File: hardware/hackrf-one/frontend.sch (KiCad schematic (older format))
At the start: 144 parts, among them J10 GND_CLIP, J2 RF-SHIELD-FRAME, J3 RF-SHIELD-COVER, J4 MOUNTING_HOLE, J5 MOUNTING_HOLE, J6 MOUNTING_HOLE, J7 MOUNTING_HOLE, J8 MOUNTING_HOLE, J9 MOUNTING_HOLE, P13 GPO1, P17 GPO6, P19 GPO3, P21 REF_IN, P27 MIXER_SDATA, P31 MIXER_SCLK, P32 MIXER_ENX, P33 MIXER_RESETX, P34 MIX_BYPASS, P35 !MIX_BYPASS, P4 ANTENNA, P42 TX, P43 RX, P44 HP, P45 LP, P46 TX_MIX_BP, P47 RX_MIX_BP, P48 TX_AMP, P49 RX_AMP, P50 AMP_BYPASS, P51 !TX_AMP_PWR, P52 !RX_AMP_PWR, P6 GPO4, P7 GPO2, Q1 MOSFET_P, Q2 MOSFET_P, Q4 MOSFET_P, T1 MIX_IN_BALUN, T2 MIX_OUT_BALUN, U1 SKY13350, U10 SKY13350, U11 SKY13350, U12 SKY13317, U13 MGA-81563, U14 SKY13317, U2 SKY13350, U25 MGA-81563, U3 RX_LOWPASS_FILTER, U4 RFFC5072, U5 SKY13350, U6 SKY13350, U7 SKY13350, U8 RX_HIGHPASS_FILTER, U9 SKY13317

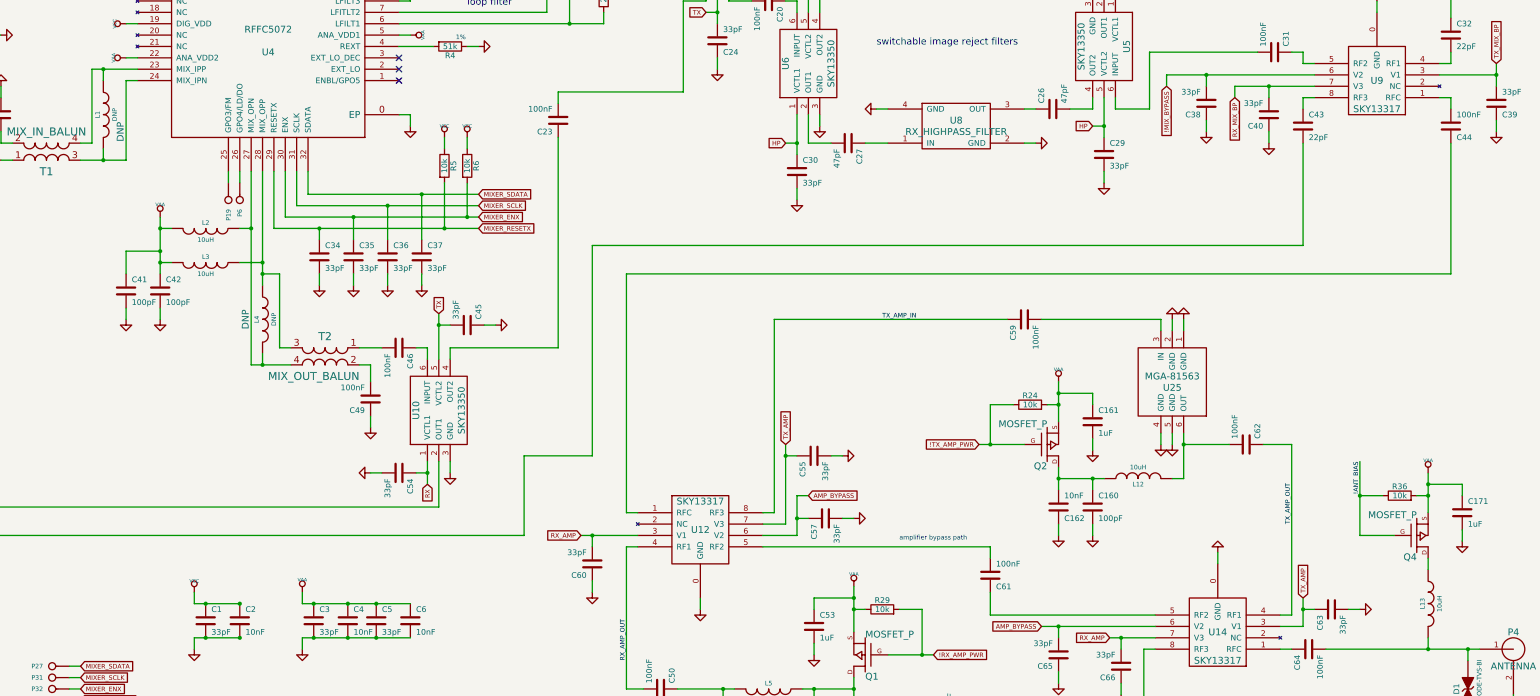
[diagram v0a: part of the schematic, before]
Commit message: HackRF One: changed U25 TX RF amplifier from MGA-81563 to TRF37A73
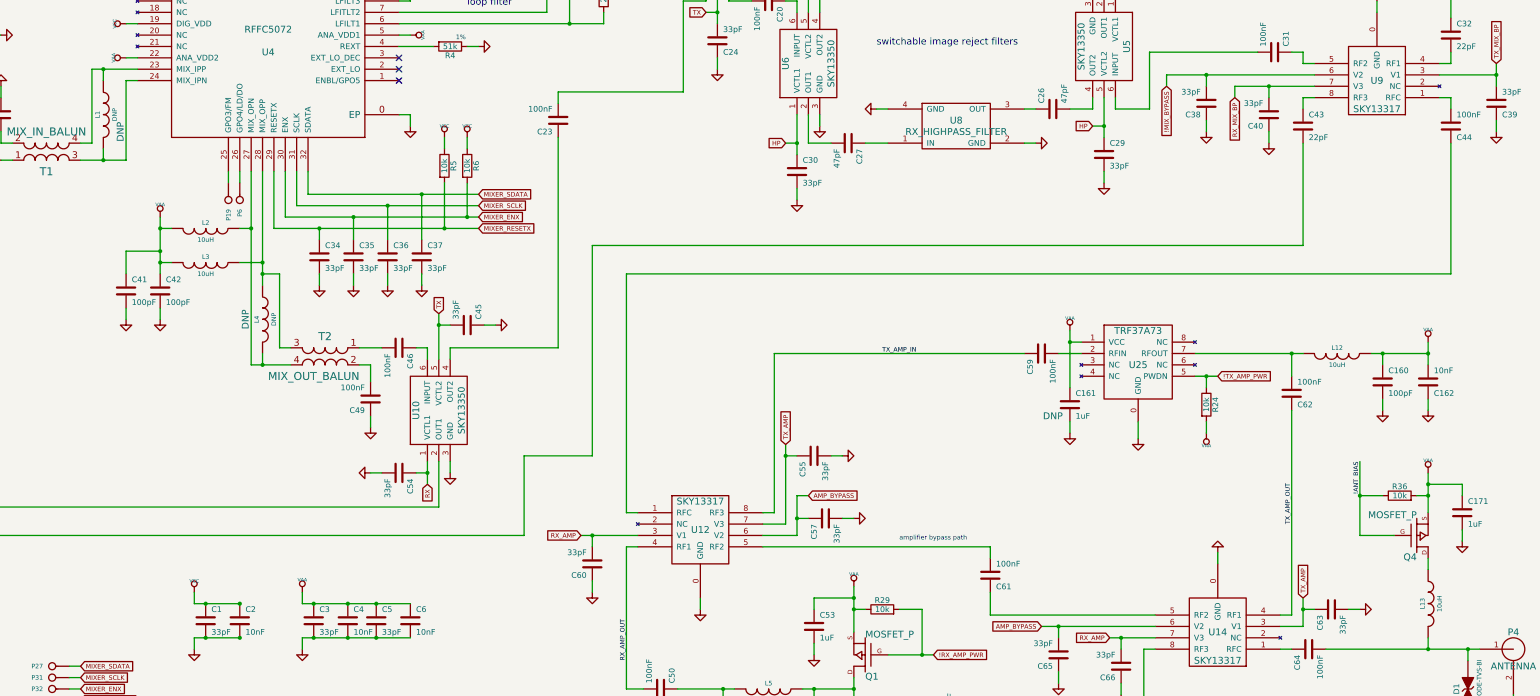
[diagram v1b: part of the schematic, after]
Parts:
- removed Q2: MOSFET_P, gsg-modules:SOT23GDS, symbol MOSFET_P
- removed U25: MGA-81563, hackrf:GSG-SOT363, symbol MGA-81563
- added U25: TRF37A73, symbol TRF37x73
- C161: Note (none) -> DNP
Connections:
- net !TX_AMP_PWR: now also U25.5 (PWDN)
- net GND: now also U25.0 (GND)
- net VAA: now also C160.1, C162.2, L12.1, U25.1 (VCC)
- net at C62.2, L12.2: now also U25.7 (RFOUT)
- net at C59.2: now also U25.2 (RFIN)
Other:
- moved on the sheet: C160, C161, C162, C59, C62, L12, R24

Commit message: HackRF One: changed U13 RX RF amplifier from MGA-81563 to TRF37D73
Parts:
- removed Q1: MOSFET_P, gsg-modules:SOT23GDS, symbol MOSFET_P
- removed U13: MGA-81563, hackrf:GSG-SOT363, symbol MGA-81563
- added U13: TRF37D73, symbol TRF37x73
- C53: Note (none) -> DNP
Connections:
- net !RX_AMP_PWR: now also R29.1, U13.5 (PWDN); no longer R29.2
- net GND: now also U13.0 (GND)
- net VAA: now also C163.2, C52.1, L5.1, R29.2, U13.1 (VCC); no longer R29.1
- net at C50.1, L5.2: now also U13.7 (RFOUT)
- net at C58.2: now also U13.2 (RFIN)
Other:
- moved on the sheet: C163, C50, C52, C53, L5, R29

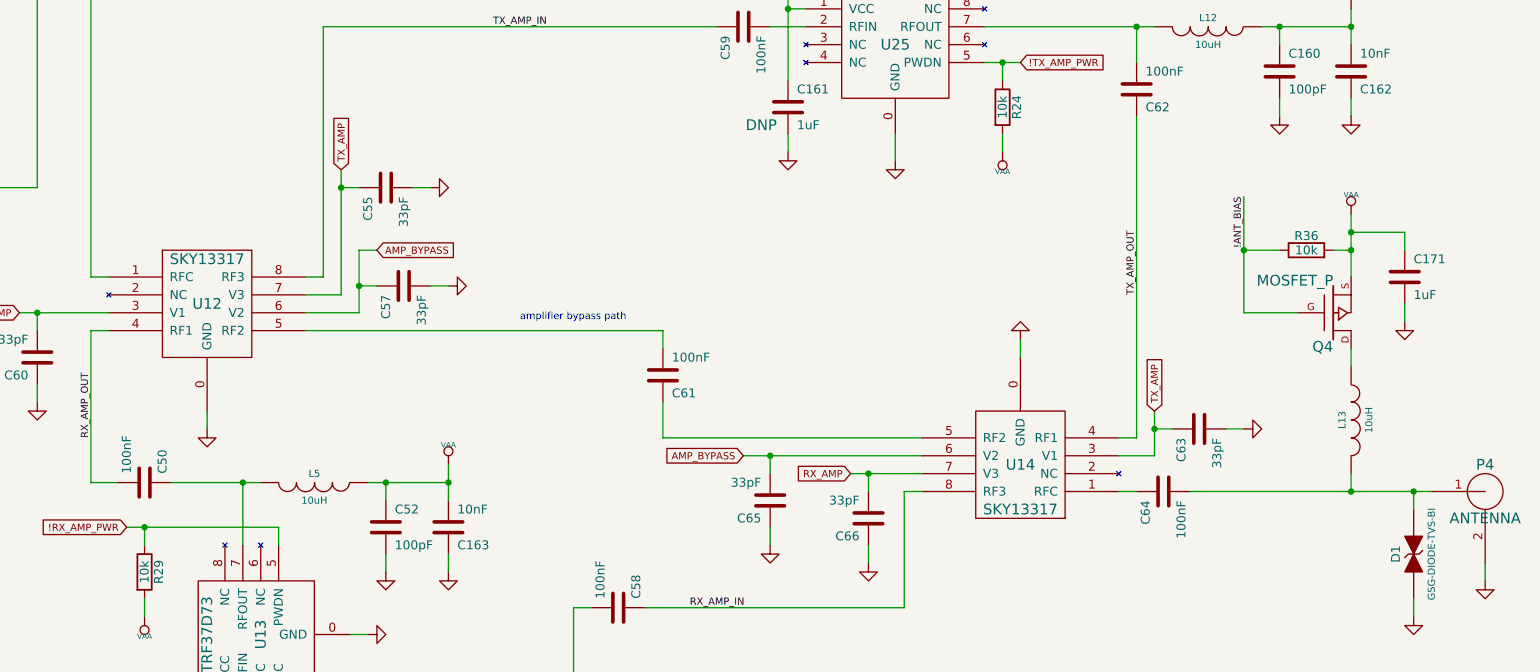
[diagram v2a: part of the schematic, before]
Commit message: HackRF One: replaced Q4 antenna port power FET with U16 current-limited power switch
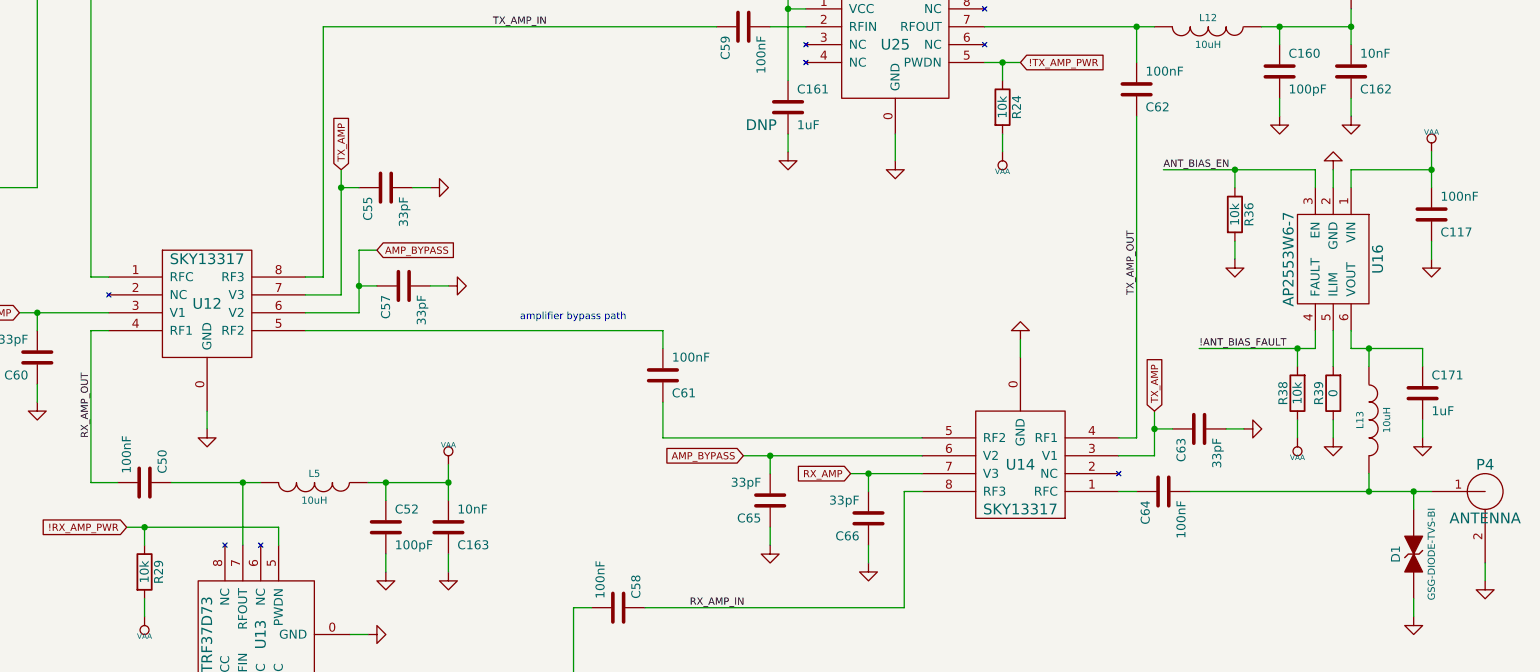
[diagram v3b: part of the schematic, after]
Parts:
- removed Q4: MOSFET_P, gsg-modules:SOT23GDS, symbol MOSFET_P
- added C117: 100nF, hackrf:GSG-0402, symbol C
- added R38: 10k, hackrf:GSG-0402, symbol R
- added R39: 0, hackrf:GSG-0402, symbol R
- added U16: AP2553W6-7, symbol NX5P2553GV
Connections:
- net !ANT_BIAS: no longer R36.1
- net GND: now also R36.2, C117.1, R39.1, U16.2 (GND)
- net VAA: now also C117.2, R38.1, U16.1 (VIN); no longer C171.1, R36.2
- net at L13.1: now also C171.1, U16.6 (VOUT)
- new net: R39.2, U16.5 (ILIM)
- new net !ANT_BIAS_FAULT: R38.2, U16.4 (FAULT)
- new net ANT_BIAS_EN: R36.1, U16.3 (EN)
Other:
- moved on the sheet: C171, L13, R36

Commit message: HackRF One: replaced NRND GRM155R61A104KA01D 100 nF capacitors with GCM155R71C104KA55
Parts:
- C117, C166, C17, C18, C20, C23, C25, C28, C31, C44, C46, C49, C50, C58, C59, C61, C62, C64, C9: Description CAP CER 0.1UF 10V 10% X5R 0402 -> CAP CER 0.1UF 16V 10% X7R 0402; Part Number GRM155R61A104KA01D -> GCM155R71C104KA55

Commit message: HackRF One: replaced NRND GRM1555C1H330JA01D 33 pF capacitors with GCM1555C1H330JA16
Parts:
- C1, C10, C11, C16, C19, C22, C24, C29, C3, C30, C33, C34, C35, C36, C37, C38, C39, C40, C45, C47, C5, C54, C55, C56, C57, C60, C63, C65, C66, C67, C7: Part Number GRM1555C1H330JA01D -> GCM1555C1H330JA16

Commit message: HackRF One: replaced obsolete LXES15AAA1-100 TVS diode with LXES15AAA1-153
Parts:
- D1: Part Number LXES15AAA1-100 -> LXES15AAA1-153
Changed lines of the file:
@@
 F 3 "" H 15900 8800 60  0001 C CNN
 F 4 "Murata" H 15900 8800 60  0001 C CNN "Manufacturer"
-F 5 "LXES15AAA1-100" H 15900 8800 60  0001 C CNN "Part Number"
+F 5 "LXES15AAA1-153" H 15900 8800 60  0001 C CNN "Part Number"
 F 6 "TVS DIODE ESD .05PF 15KV 0402" H 15900 8800 60  0001 C CNN "Description"
 	1    15900 8800

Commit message: HackRF One: replaced EoL SKY13350-385LF RF switch with SKY13453-385LF
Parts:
- removed P42: TX, hackrf:GSG-TESTPOINT-50MIL, symbol CONN_1
- removed U10, U11, U2, U5, U6, U7: SKY13350, hackrf:GSG-SKY13350-385LF, symbol SKY13350
- added U10, U11, U2, U5, U6, U7: SKY13453, hackrf:GSG-SKY13350-385LF, symbol SKY13453
- C10, C16, C19, C22, C30, C54, C56: value 33pF -> 10nF; Description CAP CER 33PF 50V 5% NP0 0402 -> CAP CER 10000PF 16V 10% X7R 0402; Part Number GCM1555C1H330JA16 -> GRM155R71C103KA01D
- U1: value SKY13350 -> SKY13453; symbol SKY13350 -> SKY13453; Description 0.01-6.0 GHz GaAs SPDT Switch -> IC SWITCH SP2T 0.01-6GHZ 6QFN; Part Number SKY13350-385LF -> SKY13453-385LF
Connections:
- net !ANT_BIAS is gone; now on net ANT_BIAS_EN: P13.1, U4.15 (GPO1/ADD1)
- net TX is gone; now on net RX: C24.2, C33.1, C45.2
- net !MIX_BYPASS: now also C7.2, U1.5 (VCTL); no longer C16.1, C47.2, U1.1 (VCTL1)
- net GND: now also C16.1, C30.1, C54.1, C56.1, U10.3 (GND), U11.3 (GND), U2.3 (GND), U5.3 (GND), U6.3 (GND), U7.3 (GND); no longer C16.2, C30.2, C54.2, C56.2
- net HP: now also C11.2, U6.5 (VCTL); no longer C29.1, C30.1
- net LP: now also C29.1, U5.5 (VCTL); no longer C11.2, C19.2
- net MIX_BYPASS: now also C47.2, U11.5 (VCTL); no longer C56.1, C7.2, U1.5 (VCTL2)
- net RX: now also U10.5 (VCTL), U2.5 (VCTL), U7.5 (VCTL); no longer C10.2, C22.2, C54.1
- net VAA: now also C10.2, C16.2, C19.2, C22.2, C30.2, C54.2, C56.2, U1.1 (VDD), U10.1 (VDD), U11.1 (VDD), U2.1 (VDD), U5.1 (VDD), U6.1 (VDD), U7.1 (VDD)
- net at C26.2: now also U5.4 (RF2)
- net at C27.2: now also U6.2 (RF1)
- net at C17.2: now also U6.4 (RF2)
- net at C20.1: now also U6.6 (RFC)
- net at C43.2: now also U11.2 (RF1)
- net at C51.1: now also U11.4 (RF2)
- net at C48.1: now also U11.6 (RFC)
- net at C51.2: now also U10.2 (RF1)
- net at C21.2: now also U7.4 (RF2)
- net at C18.1: now also U5.2 (RF1)
- net at C31.2: now also U5.6 (RFC)
- net at C20.2: now also U2.6 (RFC)
- net at C28.2: now also U7.6 (RFC)
- net at C9.1: now also U7.2 (RF1)
- net at C9.2: now also U2.2 (RF1)
- net at C23.2: now also U2.4 (RF2)
- net at C46.1: now also U10.6 (RFC)
- net at C23.1: now also U10.4 (RF2)
